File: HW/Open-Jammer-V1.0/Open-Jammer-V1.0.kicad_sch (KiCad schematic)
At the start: 0 parts

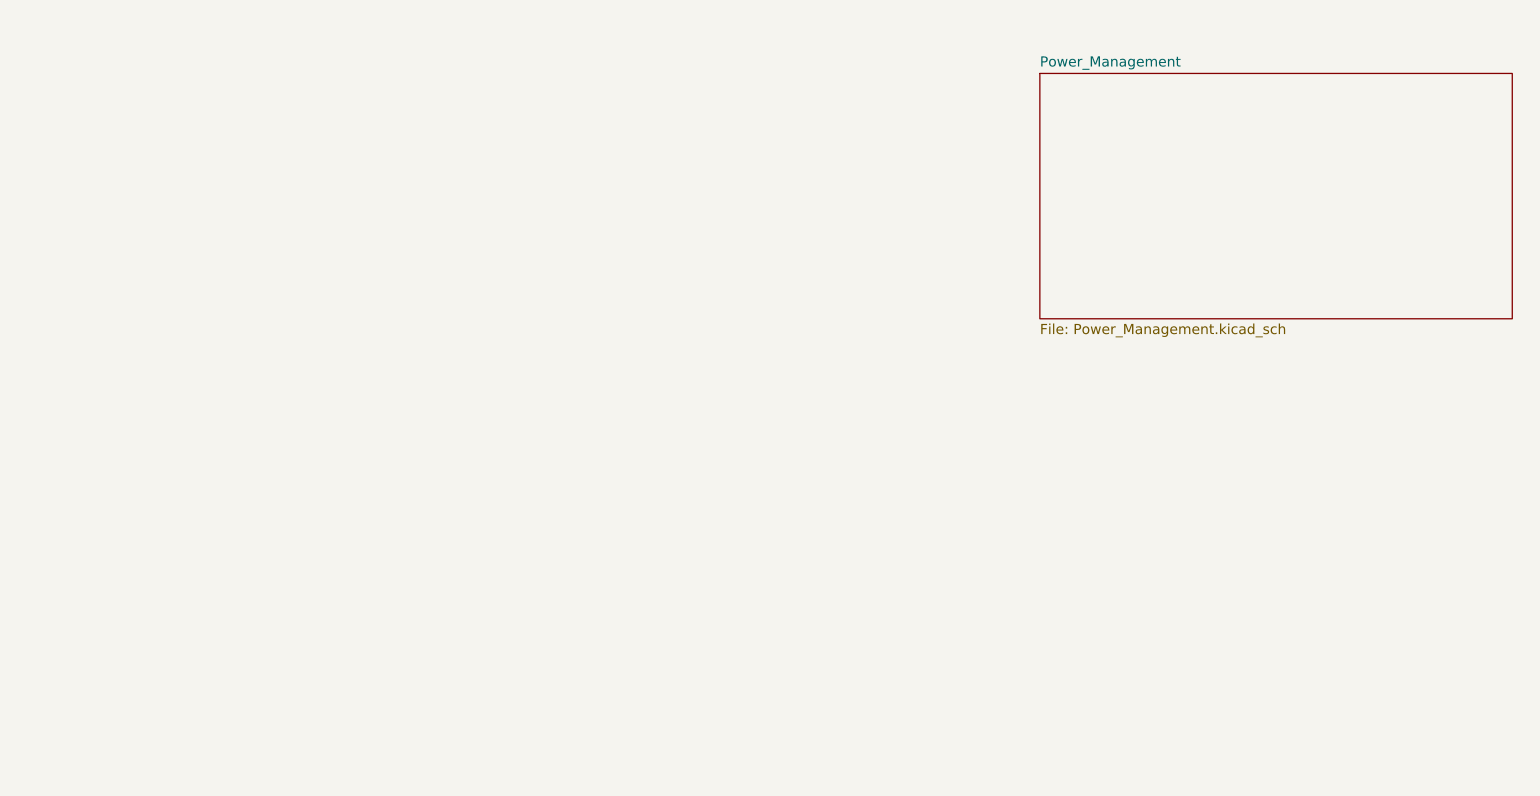
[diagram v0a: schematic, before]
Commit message: advances in schematics
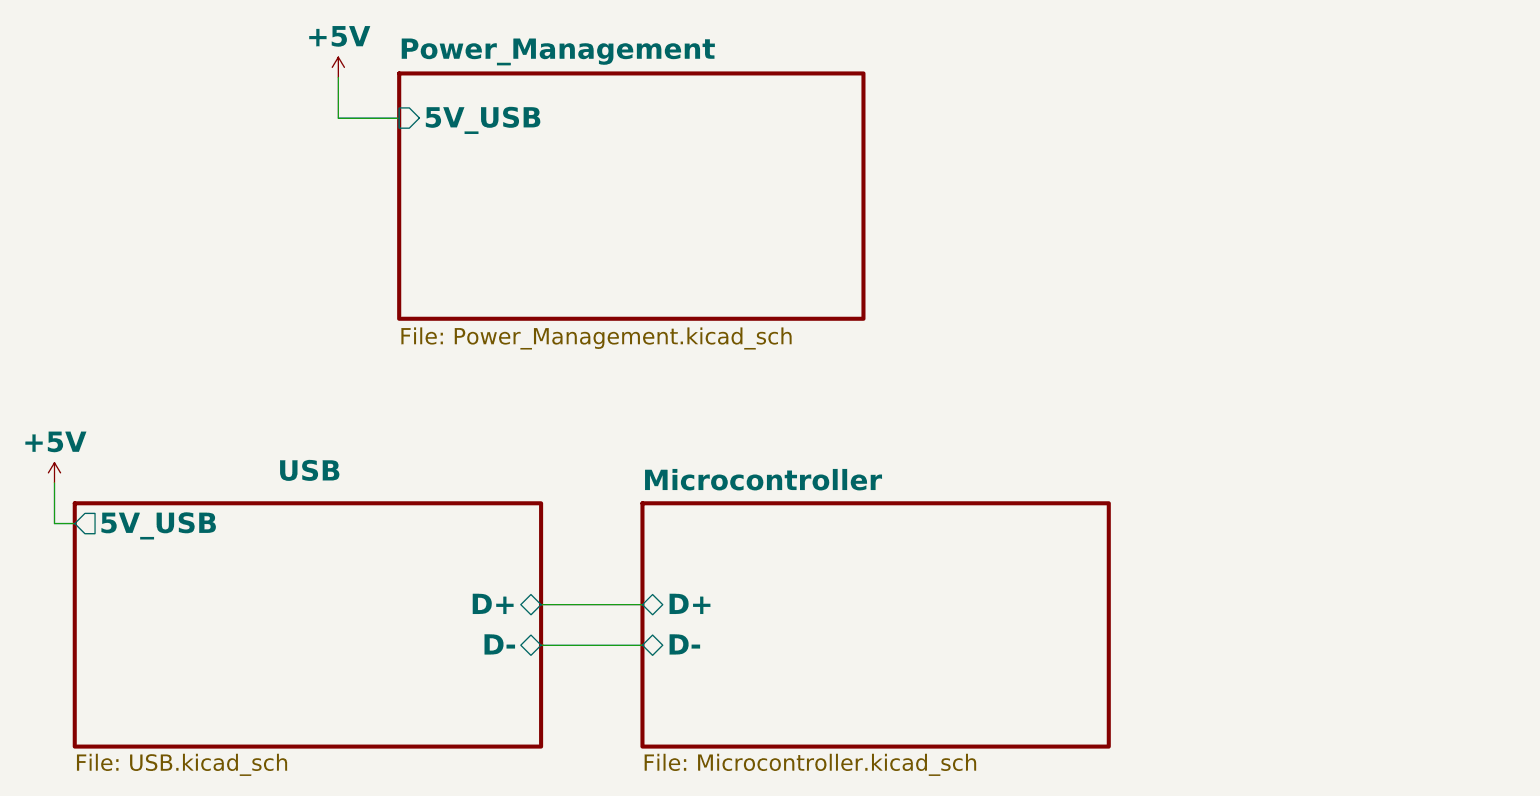
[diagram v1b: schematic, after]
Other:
- added sheet Microcontroller (Microcontroller.kicad_sch)
- added sheet USB (USB.kicad_sch)
- sheet Power_Management ports: added 5V_USB; removed none

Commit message: Added reset and boot buttons. Added oled screen. Added ESP32 VCC capacitors
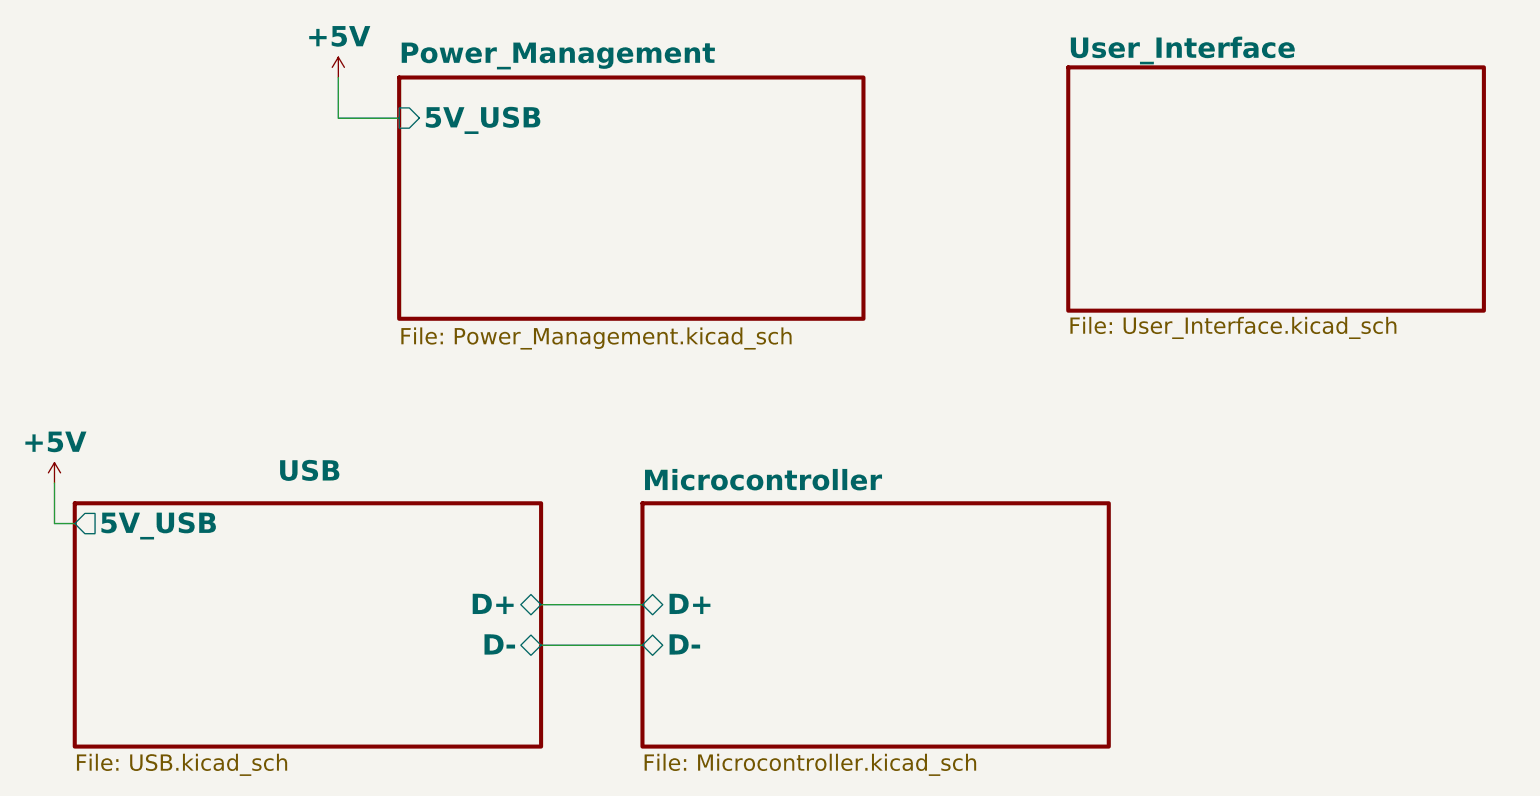
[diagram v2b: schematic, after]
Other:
- added sheet User_Interface (User_Interface.kicad_sch)
- title: (none) -> Oper Jammer V1R0
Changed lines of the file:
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@@
 	(generator_version "9.0")
 	(paper "A4")
+	(title_block
+		(title "Oper Jammer V1R0")
+		(rev "V1R0")
+	)
 	(wire
 		(pts
@@
 	)
 	(sheet
-		(at 91.44 47.752)
-		(size 58.166 30.734)
+		(at 91.44 48.26)
+		(size 58.166 30.226)
 		(exclude_from_sim no)
 		(in_bom yes)
@@
 		)
 		(property "Sheetname" "Power_Management"
-			(at 91.44 46.2276 0)
+			(at 91.44 46.7356 0)
 			(effects
 				(font
@@
 				)
 			)
+		)
+	)
+	(sheet
+		(at 175.26 46.99)
+		(size 52.07 30.48)
+		(exclude_from_sim no)
+		(in_bom yes)
+		(on_board yes)
+		(dnp no)
+		(fields_autoplaced yes)
+		(stroke
+			(width 0.508)
+			(type solid)
+			(color 0 0 0 1)
+		)
+		(fill
+			(color 0 0 0 0.0000)
+		)
+		(property "Sheetname" "User_Interface"
+			(at 175.26 46.1006 0)
+			(effects
+				(font
+					(size 2.54 2.54)
+					(thickness 0.508)
+					(bold yes)
+				)
+				(justify left bottom)
+			)
+		)
+		(property "Sheetfile" "User_Interface.kicad_sch"
+			(at 175.26 78.2324 0)
+			(effects
+				(font
+					(size 2.032 2.032)
+				)
+				(justify left top)
+			)
+		)
+		(instances
+			(project "Open-Jammer-V1.0"
+				(path "/b23e48e3-251d-4338-80a5-5d786007ffce"
+					(page "5")
+				)
+			)
